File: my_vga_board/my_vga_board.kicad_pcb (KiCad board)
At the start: 4 copper layers, 53.3 x 96 mm, 23 parts, among them J1 Barrel_Jack, J2 L77HDE15SD1CH4F, U1 Pico, U2 LM7805_TO220

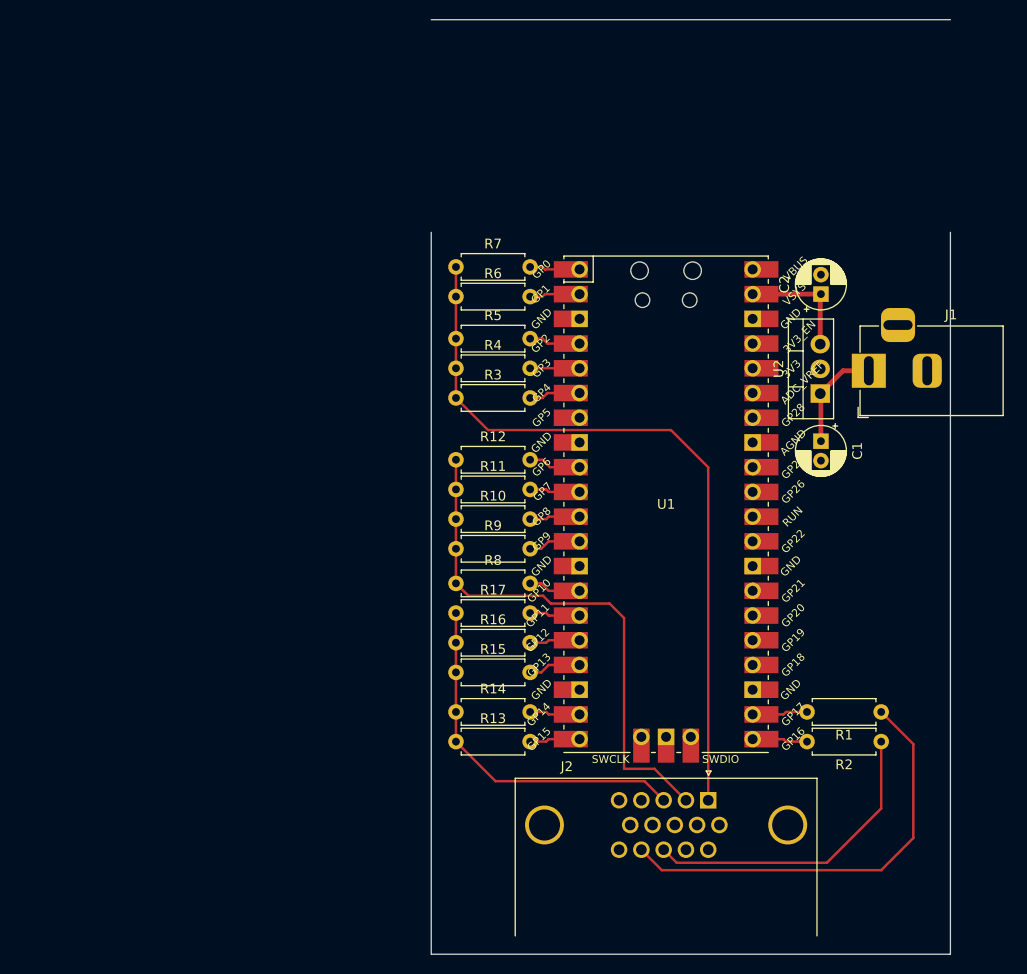
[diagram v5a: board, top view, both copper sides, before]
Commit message: now supports multiplayer... over I2C?
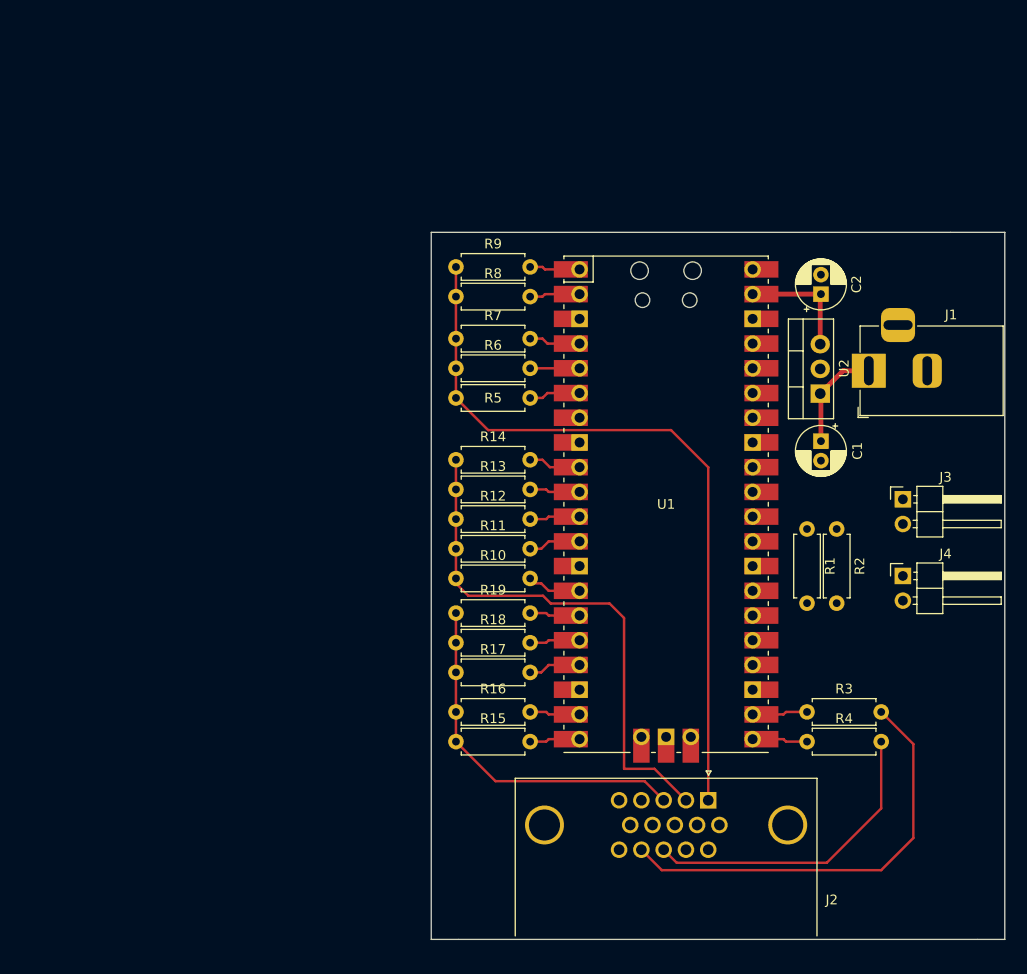
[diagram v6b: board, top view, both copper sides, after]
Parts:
- added J3: I2C_A, Connector_PinHeader_2.54mm:PinHeader_1x02_P2.54mm_Horizontal, F.Cu at (173.9, 90.4)
- added J4: I2C_B, Connector_PinHeader_2.54mm:PinHeader_1x02_P2.54mm_Horizontal, F.Cu at (173.9, 98.2)
- added R18: 4.02k, Resistor_THT:R_Axial_DIN0207_L6.3mm_D2.5mm_P7.62mm_Horizontal, F.Cu at (128.0, 105.1)
- added R19: 8.06k, Resistor_THT:R_Axial_DIN0207_L6.3mm_D2.5mm_P7.62mm_Horizontal, F.Cu at (128.0, 102.1)
- R1, R2: value 47 -> 5k
- R10, R15, R5: value 2k -> 499
- R11, R16, R6: value 4.02k -> 1k
- R12, R17, R7: value 8.06k -> 2k
- R13, R8: value 499 -> 4.02k
- R14, R9: value 1k -> 8.06k
- R3: value 499 -> 47
- R4: value 1k -> 47
- moved R4 52.6 mm to (164.1, 115.3)
- moved R3 48.4 mm to (164.1, 112.2)
- moved R8 29.5 mm to (128.0, 69.5)
- moved R9 29.0 mm to (128.0, 66.5)
- moved R13 25.9 mm to (128.0, 89.4)
- moved R14 25.9 mm to (128.0, 86.3)
- moved R2 22.3 mm to (167.1, 93.4), turned to -90 degrees
- moved R1 20.3 mm to (164.1, 93.4), turned to -90 degrees
- moved R6 7.37 mm to (128.0, 76.9)
- moved R7 7.37 mm to (128.0, 73.9)
- moved R15 7.11 mm to (128.0, 115.3)
- moved R16 7.11 mm to (128.0, 112.2)
- moved R10 6.10 mm to (128.0, 98.5)
- moved R11 6.10 mm to (128.0, 95.5)
- moved R17 6.10 mm to (128.0, 108.2)
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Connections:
- R1 pad 1: /VSYNC -> +3.3V
- R1 pad 2: /GPIO17 -> /SCL
- R10 pad 2: /GPIO8 -> /GPIO10
- R11 pad 2: /GPIO7 -> /GPIO9
- R12 pad 2: /GPIO6 -> /GPIO8
- R13 pad 1: /VGA_B -> /VGA_G
- R13 pad 2: /GPIO15 -> /GPIO7
- R14 pad 1: /VGA_B -> /VGA_G
- R14 pad 2: /GPIO14 -> /GPIO6
- R15 pad 2: /GPIO13 -> /GPIO15
- R16 pad 2: /GPIO12 -> /GPIO14
- R17 pad 2: /GPIO11 -> /GPIO13
- R2 pad 1: /HSYNC -> +3.3V
- R2 pad 2: /GPIO16 -> /SDA
- R3 pad 1: /VGA_R -> /VSYNC
- R3 pad 2: /GPIO4 -> /GPIO17
- R4 pad 1: /VGA_R -> /HSYNC
- R4 pad 2: /GPIO3 -> /GPIO16
- R5 pad 2: /GPIO2 -> /GPIO4
- R6 pad 2: /GPIO1 -> /GPIO3
- R7 pad 2: /GPIO0 -> /GPIO2
- R8 pad 1: /VGA_G -> /VGA_R
- R8 pad 2: /GPIO10 -> /GPIO1
- R9 pad 1: /VGA_G -> /VGA_R
- R9 pad 2: /GPIO9 -> /GPIO0
- U1 pad 24: unconnected-(U1-Pad24) -> /SDA
- U1 pad 25: unconnected-(U1-Pad25) -> /SCL
- U1 pad 36: unconnected-(U1-Pad36) -> +3.3V
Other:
- board size 53.3 x 96 mm -> 58.9 x 72.6 mm

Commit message: maybe can be fabbed?
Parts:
- moved R3 7.62 mm to (171.7, 112.2), turned to 180 degrees
- moved R4 7.62 mm to (171.7, 115.3), turned to 180 degrees
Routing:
- net /SDA: track 0.00 -> 29.3 mm
- net /SCL: track 0.00 -> 29.0 mm
- net +3.3V: track 0.00 -> 22.9 mm
- added copper zone on B.Cu, net GND
- added copper zone on F.Cu, net GND
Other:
- board size 58.9 x 72.6 mm -> 58.9 x 71.1 mm

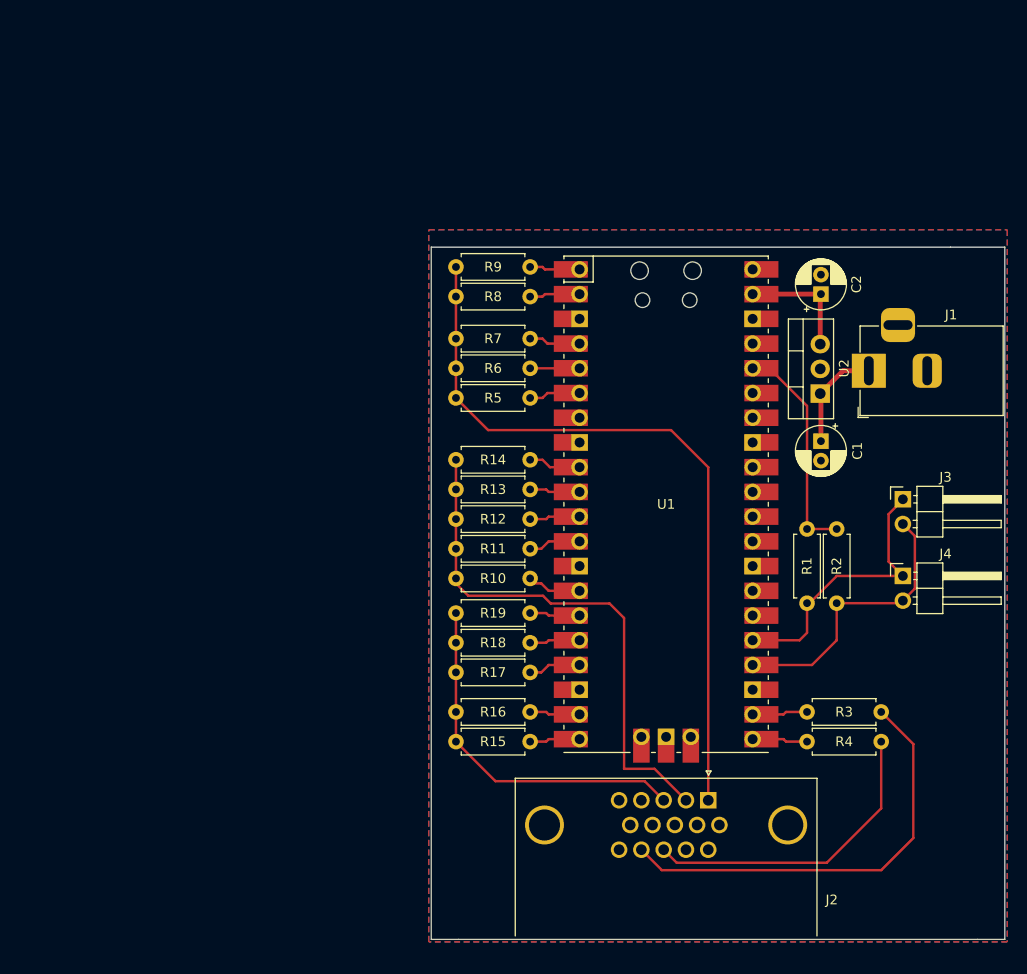
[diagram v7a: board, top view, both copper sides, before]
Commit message: now with mounting holes, and accredidation, ooooh
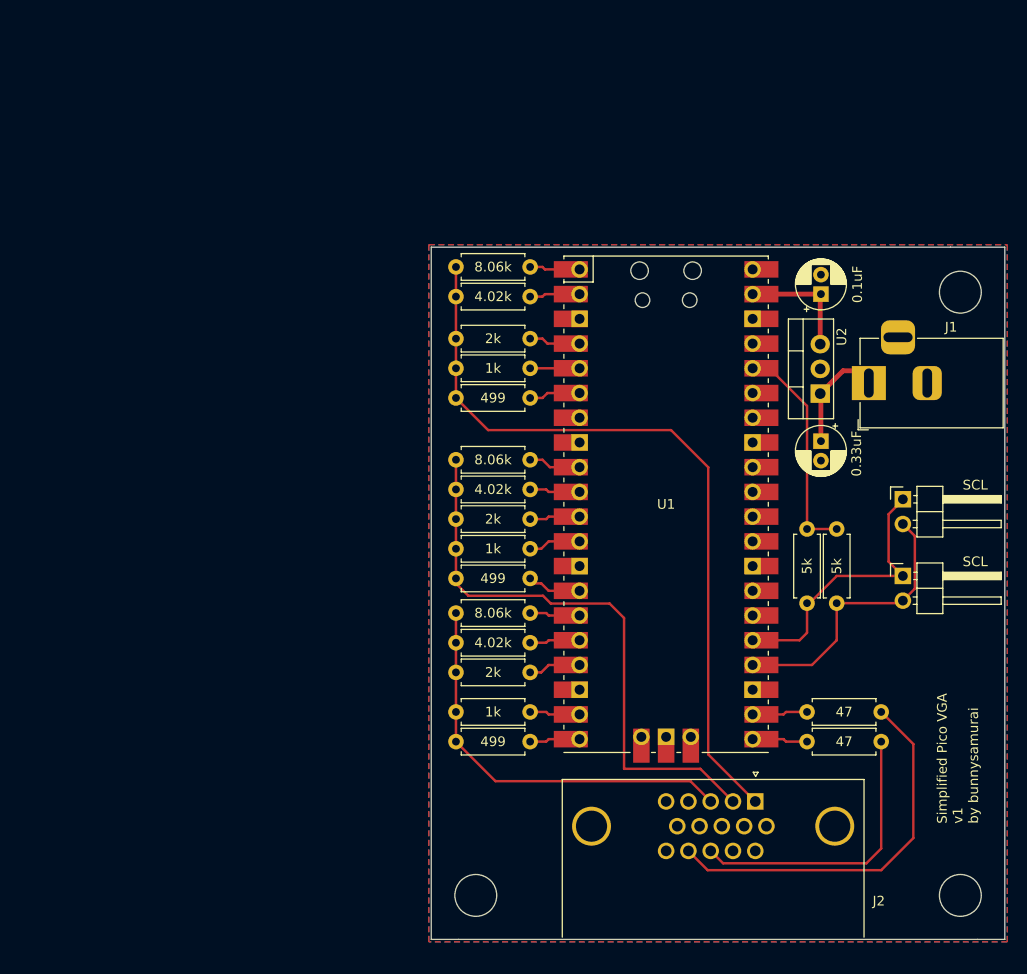
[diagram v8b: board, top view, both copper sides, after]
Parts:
- added H1: MountingHole, MountingHole:MountingHole_4.3mm_M4, F.Cu at (130.0, 131.1)
- added H2: MountingHole, MountingHole:MountingHole_4.3mm_M4, F.Cu at (179.8, 69.1)
- added H3: MountingHole, MountingHole:MountingHole_4.3mm_M4, F.Cu at (179.8, 131.1)
- moved J2 4.83 mm to (154.4, 135.4)
- moved J1 1.26 mm to (170.4, 78.4)
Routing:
- net /VGA_G: track 54.6 -> 59.5 mm
- net /VSYNC: track 44.5 -> 39.6 mm
- net /VGA_B: track 37.0 -> 41.9 mm
- net /HSYNC: track 32.1 -> 29.7 mm
- net /VGA_R: track 76.5 -> 78.7 mm
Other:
- copper layers 4 -> 2
- board text added: "SCL"
- board text added: "Simplified Pico VGA v1 by bunnysamurai"
- board text removed: "0.035mm"
- board text removed: "0.360mm"
- board text removed: "0.710mm"
- board text removed: "1.57mm"
- board text removed: "Board Stack Up"
- board text removed: "Core - FR4"
- board text removed: "Cu"
- board text removed: "Cu Plated to 35um"
- board text removed: "Details"
- board text removed: "Dielectric"
- board text removed: "L1"
- board text removed: "L2"
- board text removed: "L3"
- board text removed: "L4"
- board text removed: "Layer"
- board text removed: "Prepreg"
- board text removed: "Radius = 3mm"
- board text removed: "Thickness"
- board text removed: "Through Vias L1-4"
- board text removed: "Total"
